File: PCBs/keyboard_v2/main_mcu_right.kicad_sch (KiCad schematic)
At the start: 28 parts, among them U801 STM32U5G9ZJJ6Q, U802 M24256X-FCU6T_VF, Y801 16MHz

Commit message: V2 progress
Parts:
- removed C801, C802: 6p, Capacitor_SMD:C_0402_1005Metric, symbol Device:C_Small
- removed Y801: 16MHz, Crystal:Crystal_SMD_2016-4Pin_2.0x1.6mm, symbol Device:Crystal_GND24_Small
- added C823, C824: 12p, Capacitor_SMD:C_0402_1005Metric, symbol Device:C_Small
- added Y802: 32MHz, Crystal:Crystal_SMD_2016-4Pin_2.0x1.6mm, symbol Device:Crystal_GND24_Small
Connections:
- net GND: now also C823.1, C824.1, Y802.2, Y802.4
- net OSC_IN: now also C823.2, Y802.3
- net OSC_OUT: now also C824.2, Y802.1
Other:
- moved on the sheet: U801B

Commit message: V2 Progress
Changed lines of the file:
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@@
+		)
+	)
+	(hierarchical_label "DSI_D0P"
+		(shape bidirectional)
+		(at 185.42 139.7 0)
+		(fields_autoplaced yes)
+		(effects
+			(font
+				(size 1.27 1.27)
+			)
+			(justify left)
 		)
 	)
@@
 		)
 	)
+	(hierarchical_label "DSI_CKN"
+		(shape output)
+		(at 185.42 137.16 0)
+		(fields_autoplaced yes)
+		(effects
+			(font
+				(size 1.27 1.27)
+			)
+			(justify left)
+		)
+	)
 	(hierarchical_label "KEY_B11"
 		(shape input)
@@
 		)
 	)
+	(hierarchical_label "DSI_TE"
+		(shape input)
+		(at 185.42 132.08 0)
+		(fields_autoplaced yes)
+		(effects
+			(font
+				(size 1.27 1.27)
+			)
+			(justify left)
+		)
+	)
 	(hierarchical_label "KEY_A11"
 		(shape input)
@@
 		)
 	)
+	(hierarchical_label "USB_DN"
+		(shape bidirectional)
+		(at 185.42 119.38 0)
+		(fields_autoplaced yes)
+		(effects
+			(font
+				(size 1.27 1.27)
+			)
+			(justify left)
+		)
+	)
 	(hierarchical_label "KEY_A10"
 		(shape input)
@@
 		)
 	)
+	(hierarchical_label "DSI_D0N"
+		(shape bidirectional)
+		(at 185.42 142.24 0)
+		(fields_autoplaced yes)
+		(effects
+			(font
+				(size 1.27 1.27)
+			)
+			(justify left)
+		)
+	)
 	(hierarchical_label "KEY_A12"
 		(shape input)
@@
 		)
 	)
+	(hierarchical_label "USB_DP"
+		(shape bidirectional)
+		(at 185.42 116.84 0)
+		(fields_autoplaced yes)
+		(effects
+			(font
+				(size 1.27 1.27)
+			)
+			(justify left)
+		)
+	)
 	(hierarchical_label "KEY_B10"
 		(shape input)
@@
 		(fields_autoplaced yes)
 		(effects
+			(font
+				(size 1.27 1.27)
+			)
+			(justify left)
+		)
+	)
+	(hierarchical_label "DSI_CKP"
+		(shape output)
+		(at 185.42 134.62 0)
+		(fields_autoplaced yes)
+		(effects

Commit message: Display schematic done
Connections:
- net +1V8: now also U802.A1 (VCC); no longer U801.E6 (VDDIO2)
- net +3V3: now also U801.E6 (VDDIO2); no longer U802.A1 (VCC)
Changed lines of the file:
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@@
 	)
 	(junction
+		(at 205.74 226.06)
+		(diameter 0)
+		(color 0 0 0 0)
+	)
+	(junction
 		(at 195.58 233.68)
 		(diameter 0)
@@
 	)
 	(junction
+		(at 205.74 218.44)
+		(diameter 0)
+		(color 0 0 0 0)
+	)
+	(junction
 		(at 256.54 215.9)
 		(diameter 0)
@@
 	)
 	(junction
-		(at 205.74 226.06)
-		(diameter 0)
-		(color 0 0 0 0)
-	)
-	(junction
 		(at 53.34 246.38)
 		(diameter 0)
@@
 	)
 	(junction
-		(at 205.74 218.44)
-		(diameter 0)
-		(color 0 0 0 0)
-	)
-	(junction
 		(at 256.54 243.84)
 		(diameter 0)
@@
 	)
 	(junction
-		(at 205.74 223.52)
-		(diameter 0)
-		(color 0 0 0 0)
-	)
-	(junction
 		(at 205.74 233.68)
 		(diameter 0)
@@
 	(wire
 		(pts
+			(xy 205.74 226.06) (xy 205.74 228.6)
+		)
+		(stroke
+			(width 0)
+			(type default)
+		)
+	)
+	(wire
+		(pts
 			(xy 256.54 205.74) (xy 254 205.74)
 		)
@@
 	(wire
 		(pts
+			(xy 208.28 226.06) (xy 205.74 226.06)
+		)
+		(stroke
+			(width 0)
+			(type default)
+		)
+	)
+	(wire
+		(pts
 			(xy 256.54 218.44) (xy 256.54 220.98)
 		)
@@
 	(wire
 		(pts
-			(xy 205.74 226.06) (xy 205.74 228.6)
-		)
-		(stroke
-			(width 0)
-			(type default)
-		)
-	)
-	(wire
-		(pts
 			(xy 256.54 200.66) (xy 254 200.66)
 		)
@@
 	(wire
 		(pts
-			(xy 205.74 223.52) (xy 205.74 226.06)
-		)
-		(stroke
-			(width 0)
-			(type default)
-		)
-	)
-	(wire
-		(pts
 			(xy 386.08 238.76) (xy 388.62 238.76)
 		)
@@
 	(wire
 		(pts
+			(xy 200.66 223.52) (xy 208.28 223.52)
+		)
+		(stroke
+			(width 0)
+			(type default)
+		)
+	)
+	(wire
+		(pts
 			(xy 205.74 205.74) (xy 208.28 205.74)
 		)
@@
 	(wire
 		(pts
-			(xy 205.74 223.52) (xy 208.28 223.52)
+			(xy 205.74 218.44) (xy 205.74 226.06)
 		)
 		(stroke
@@
 	(wire
 		(pts
+			(xy 200.66 220.98) (xy 200.66 223.52)
+		)
+		(stroke
+			(width 0)
+			(type default)
+		)
+	)
+	(wire
+		(pts
 			(xy 256.54 228.6) (xy 256.54 233.68)
 		)
@@
 	(wire
 		(pts
-			(xy 205.74 218.44) (xy 205.74 223.52)
-		)
-		(stroke
-			(width 0)
-			(type default)
-		)
-	)
-	(wire
-		(pts
 			(xy 73.66 220.98) (xy 83.82 220.98)
 		)
@@
 	(wire
 		(pts
-			(xy 205.74 226.06) (xy 208.28 226.06)
-		)
-		(stroke
-			(width 0)
-			(type default)
-		)
-	)
-	(wire
-		(pts
 			(xy 63.5 254) (xy 63.5 256.54)
 		)
@@
 	(symbol
 		(lib_id "power:+3V3")
+		(at 200.66 220.98 0)
+		(unit 1)
+		(exclude_from_sim no)
+		(in_bom yes)
+		(on_board yes)
+		(dnp no)
+		(fields_autoplaced yes)
+		(property "Reference" "#PWR0805"
+			(at 200.66 224.79 0)
+			(effects
+				(font
+					(size 1.27 1.27)
+				)
+				(hide yes)
+			)
+		)
+		(property "Value" "+3V3"
+			(at 200.66 217.17 0)
+			(effects
+				(font
+					(size 1.27 1.27)
+				)
+			)
+		)
+		(property "Footprint" ""
+			(at 200.66 220.98 0)
+			(effects
+				(font
+					(size 1.27 1.27)
+				)
+				(hide yes)
+			)
+		)
+		(property "Datasheet" ""
+			(at 200.66 220.98 0)
+			(effects
+				(font
+					(size 1.27 1.27)
+				)
+				(hide yes)
+			)
+		)
+		(property "Description" "Power symbol creates a global label with name \"+3V3\""
+			(at 200.66 220.98 0)
+			(effects
+				(font
+					(size 1.27 1.27)
+				)
+				(hide yes)
+			)
+		)
+		(pin "1"
+		)
+		(instances
+			(project "keyboard_v2"
+				(path "/e2360b7f-be71-48d9-b398-9f8cd45479d6/b599252a-0e44-4760-9c79-385d4380db60/c45c2f49-4b68-419d-a43d-2f217736a467"
+					(reference "#PWR0805")
+					(unit 1)
+				)
+			)
+		)
+	)
+	(symbol
+		(lib_id "power:+3V3")
 		(at 251.46 40.64 0)
 		(unit 1)
@@
 	)
 	(symbol
+		(lib_id "power:+1V8")
+		(at 388.62 233.68 0)
+		(mirror y)
+		(unit 1)
+		(exclude_from_sim no)
+		(in_bom yes)
+		(on_board yes)
+		(dnp no)
+		(fields_autoplaced yes)
+		(property "Reference" "#PWR0803"
+			(at 388.62 237.49 0)
+			(effects
+				(font
+					(size 1.27 1.27)
+				)
+				(hide yes)
+			)
+		)
+		(property "Value" "+1V8"
+			(at 388.62 228.6 0)
+			(effects
+				(font
+					(size 1.27 1.27)
+				)
+			)
+		)
+		(property "Footprint" ""
+			(at 388.62 233.68 0)
+			(effects
+				(font
+					(size 1.27 1.27)
+				)
+				(hide yes)
+			)
+		)
+		(property "Datasheet" ""
+			(at 388.62 233.68 0)
+			(effects
+				(font
+					(size 1.27 1.27)
+				)
+				(hide yes)
+			)
+		)
+		(property "Description" "Power symbol creates a global label with name \"+1V8\""
+			(at 388.62 233.68 0)
+			(effects
+				(font
+					(size 1.27 1.27)
+				)
+				(hide yes)
+			)
+		)
+		(pin "1"
+		)
+		(instances
+			(project "keyboard_v2"
+				(path "/e2360b7f-be71-48d9-b398-9f8cd45479d6/b599252a-0e44-4760-9c79-385d4380db60/c45c2f49-4b68-419d-a43d-2f217736a467"
+					(reference "#PWR0803")
+					(unit 1)
+				)
+			)
+		)
+	)
+	(symbol
 		(lib_id "M24256X-FCU6T_VF:M24256X-FCU6T_VF")
 		(at 373.38 236.22 0)
@@
 					(unit 1)
 				)
-			)
-		)
-	)
-	(symbol
-		(lib_id "power:+3V3")
-		(at 388.62 233.68 0)
-		(unit 1)
-		(exclude_from_sim no)
-		(in_bom yes)
-		(on_board yes)
-		(dnp no)
-		(fields_autoplaced yes)
-		(property "Reference" "#PWR0803"
-			(at 388.62 237.49 0)
-			(effects
-				(font
-					(size 1.27 1.27)
-				)
-				(hide yes)
-			)
-		)
-		(property "Value" "+3V3"
-			(at 388.62 228.6 0)
-			(effects
-				(font
-					(size 1.27 1.27)
-				)
-			)
-		)
-		(property "Footprint" ""
-			(at 388.62 233.68 0)
-			(effects
-				(font
-					(size 1.27 1.27)
-				)
-				(hide yes)
-			)
-		)
-		(property "Datasheet" ""
-			(at 388.62 233.68 0)
-			(effects
-				(font
-					(size 1.27 1.27)
-				)
-				(hide yes)
-			)
-		)
-		(property "Description" "Power symbol creates a global label with name \"+3V3\""
-			(at 388.62 233.68 0)
-			(effects
-				(font
-					(size 1.27 1.27)
-				)
-				(hide yes)
-			)
-		)
-		(pin "1"
-		)
-		(instances
-			(project "keyboard_v2"
-				(path "/e2360b7f-be71-48d9-b398-9f8cd45479d6/b599252a-0e44-4760-9c79-385d4380db60/c45c2f49-4b68-419d-a43d-2f217736a467"
-					(reference "#PWR0803")
-					(unit 1)
-				)

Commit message: V2 Schematic mostly done
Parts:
- U802: footprint watch_footprints:BGA4C50P2X2_70X98X33 -> keyboard_footprints:BGA4C50P2X2_70X98X33
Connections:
- net +1V8: now also R801.1, R802.1; no longer C813.1, C815.1
- net +3V3: now also C813.1, C815.1; no longer R801.1, R802.1
- net DSI_CKN: now also U801.F1 (DSI_CKN)
- net DSI_CKP: now also U801.F2 (DSI_CKP)
- net DSI_D0N: now also U801.E1 (DSI_D0N)
- net DSI_D0P: now also U801.E2 (DSI_D0P)
- net OSC_IN: now also U801.H2 (PH0-OSC_IN)
- net OSC_OUT: now also U801.J1 (PH1-OSC_OUT)
- net RST: now also U801.J2 (NRST)
- no-connect marks 0 -> 2
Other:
- note added: "ENCODER PINS MUST BE 5V TOLERANT"
- moved on the sheet: U801B

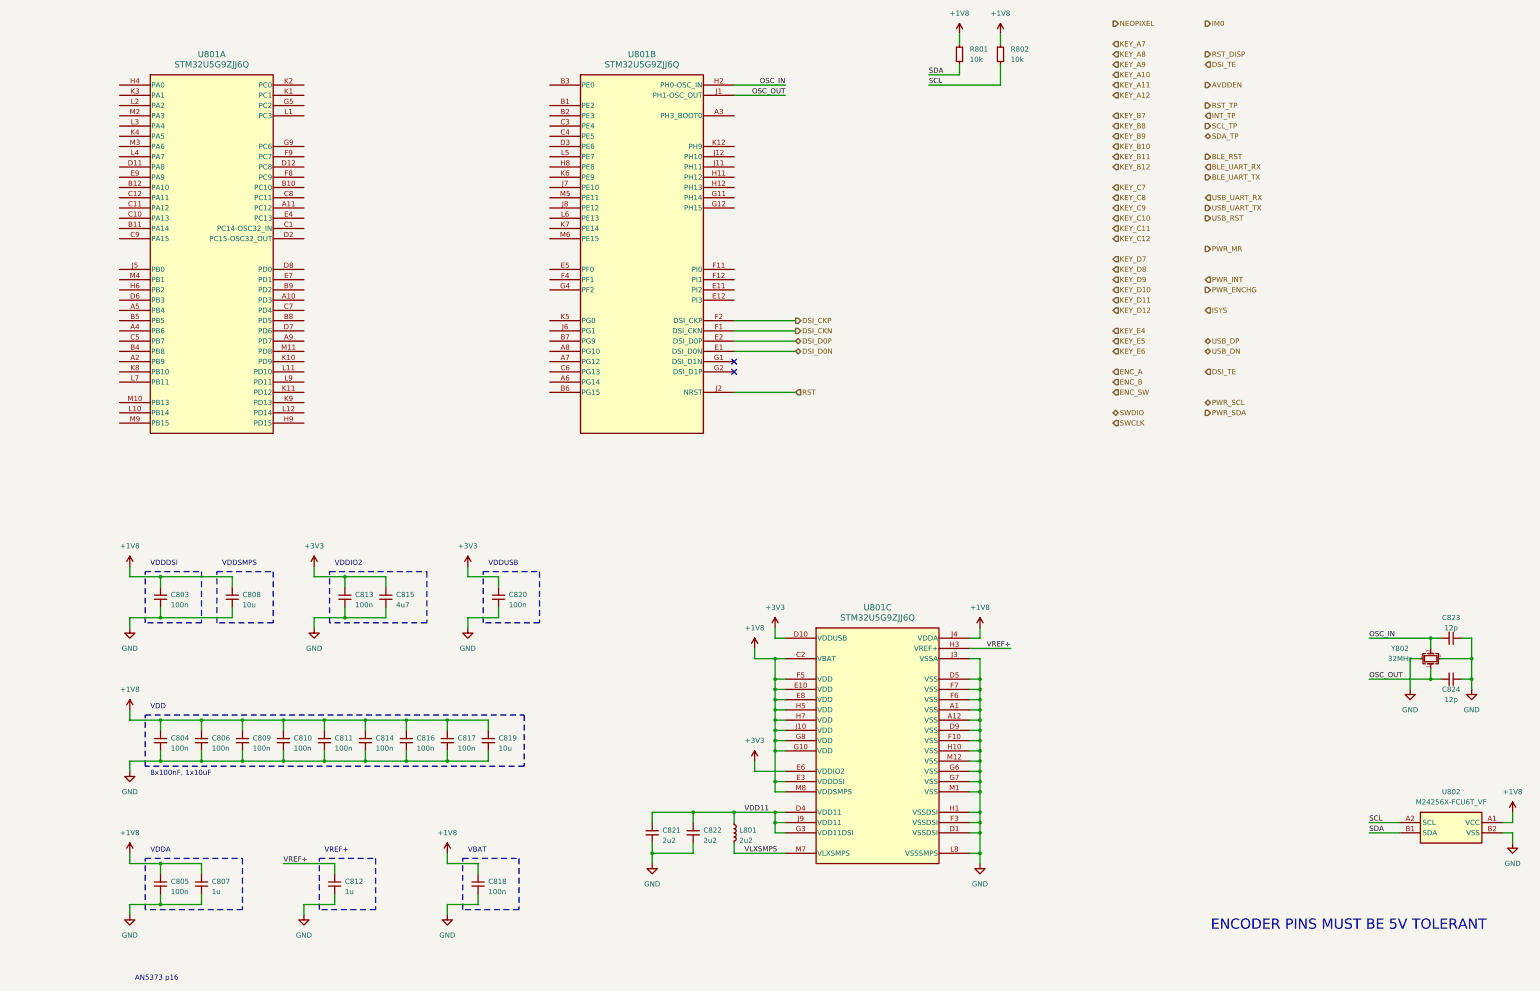
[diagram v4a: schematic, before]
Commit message: Schematic mostly done, moving onto PCB
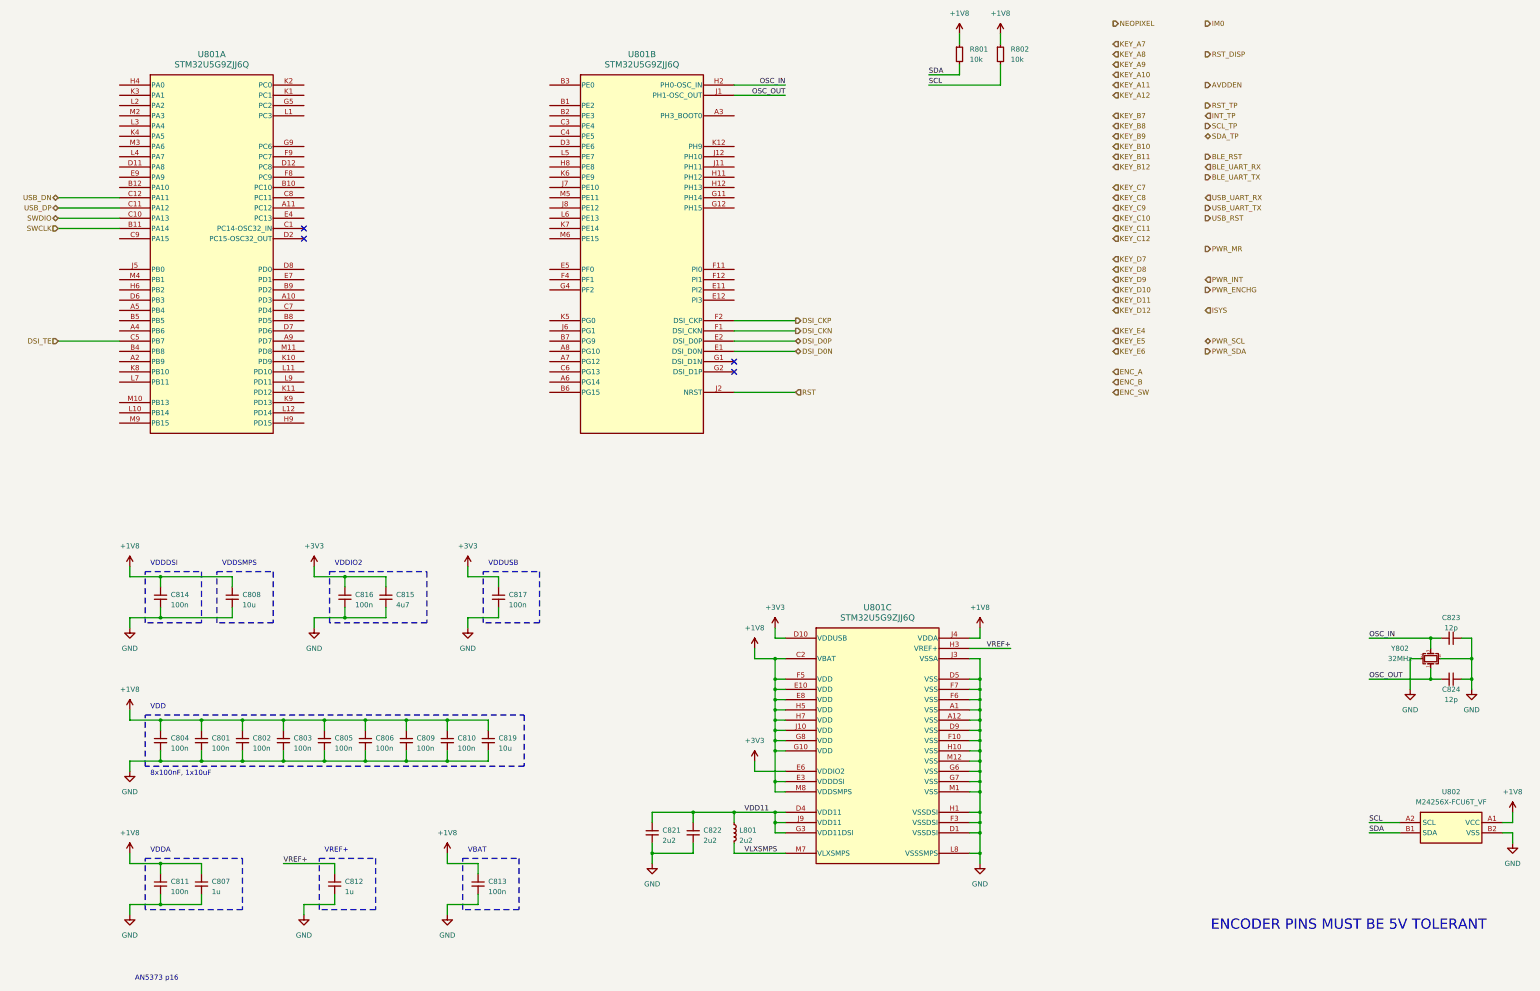
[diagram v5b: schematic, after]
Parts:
- removed C818, C820: 100n, Capacitor_SMD:C_0201_0603Metric, symbol Device:C_Small
- added C801, C802: 100n, Capacitor_SMD:C_0402_1005Metric, symbol Device:C_Small
- C803, C804, C805, C806, C809, C810, C811, C812, C813, C814, C816, C817, C821, C822: footprint Capacitor_SMD:C_0201_0603Metric -> Capacitor_SMD:C_0402_1005Metric
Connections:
- net +1V8: now also C813.1, C801.1, C802.1; no longer C816.1, C817.1
- net +3V3: now also C816.1, C817.1; no longer C813.1
- net DSI_TE: now also U801.C5 (PB7)
- net GND: now also C801.2, C802.2
- net SWCLK: now also U801.B11 (PA14)
- net SWDIO: now also U801.C10 (PA13)
- net USB_DN: now also U801.C12 (PA11)
- net USB_DP: now also U801.C11 (PA12)
- no-connect marks 2 -> 4

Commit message: Placement done
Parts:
- C807: footprint Capacitor_SMD:C_0201_0603Metric -> Capacitor_SMD:C_0402_1005Metric
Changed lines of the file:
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@@
 			)
 		)
-		(property "Footprint" "Capacitor_SMD:C_0201_0603Metric"
+		(property "Footprint" "Capacitor_SMD:C_0402_1005Metric"
 			(at 63.5 251.46 0)
 			(effects

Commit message: 279 Unrouted
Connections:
- net SCL is gone; now on net PWR_SCL: R802.2, U802.A2 (SCL)
- net SDA is gone; now on net PWR_SDA: R801.2, U802.B1 (SDA)
- net AVDDEN: now also U801.L1 (PC3)
- net BLE_UART_RX: now also U801.K10 (PD9)
- net BLE_UART_TX: now also U801.M11 (PD8)
- net IM0: now also U801.B1 (PE2)
- net INT_TP: now also U801.L2 (PA2)
- net NEOPIXEL: now also U801.M9 (PB15)
- net RST_DISP: now also U801.K2 (PC0)
- net RST_TP: now also U801.A7 (PG12)
- net SCL_TP: now also U801.A6 (PG14)
- net SDA_TP: now also U801.C6 (PG13)
- no-connect marks 4 -> 5
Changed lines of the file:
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@@
+	)
+	(no_connect
+		(at 43.18 132.08)
 	)
 	(no_connect
@@
 	(wire
 		(pts
+			(xy 88.9 60.96) (xy 99.06 60.96)
+		)
+		(stroke
+			(width 0)
+			(type default)
+		)
+	)
+	(wire
+		(pts
 			(xy 63.5 210.82) (xy 73.66 210.82)
 		)
@@
 	(wire
 		(pts
+			(xy 88.9 121.92) (xy 101.6 121.92)
+		)
+		(stroke
+			(width 0)
+			(type default)
+		)
+	)
+	(wire
+		(pts
+			(xy 325.12 119.38) (xy 335.28 119.38)
+		)
+		(stroke
+			(width 0)
+			(type default)
+		)
+	)
+	(wire
+		(pts
 			(xy 185.42 233.68) (xy 185.42 236.22)
 		)
@@
 	(wire
 		(pts
+			(xy 139.7 124.46) (xy 149.86 124.46)
+		)
+		(stroke
+			(width 0)
+			(type default)
+		)
+	)
+	(wire
+		(pts
 			(xy 45.72 220.98) (xy 53.34 220.98)
 		)
@@
 	(wire
 		(pts
+			(xy 27.94 137.16) (xy 43.18 137.16)
+		)
+		(stroke
+			(width 0)
+			(type default)
+		)
+	)
+	(wire
+		(pts
 			(xy 205.74 195.58) (xy 205.74 200.66)
 		)
@@
 	(wire
 		(pts
+			(xy 139.7 127) (xy 149.86 127)
+		)
+		(stroke
+			(width 0)
+			(type default)
+		)
+	)
+	(wire
+		(pts
 			(xy 386.08 238.76) (xy 388.62 238.76)
 		)
@@
 	(wire
 		(pts
+			(xy 137.16 58.42) (xy 149.86 58.42)
+		)
+		(stroke
+			(width 0)
+			(type default)
+		)
+	)
+	(wire
+		(pts
 			(xy 88.9 256.54) (xy 96.52 256.54)
 		)
@@
 	(wire
 		(pts
+			(xy 27.94 58.42) (xy 43.18 58.42)
+		)
+		(stroke
+			(width 0)
+			(type default)
+		)
+	)
+	(wire
+		(pts
 			(xy 114.3 210.82) (xy 124.46 210.82)
 		)
@@
 	(wire
 		(pts
+			(xy 325.12 116.84) (xy 335.28 116.84)
+		)
+		(stroke
+			(width 0)
+			(type default)
+		)
+	)
+	(wire
+		(pts
 			(xy 200.66 223.52) (xy 208.28 223.52)
 		)
@@
 	(wire
 		(pts
+			(xy 88.9 119.38) (xy 101.6 119.38)
+		)
+		(stroke
+			(width 0)
+			(type default)
+		)
+	)
+	(wire
+		(pts
 			(xy 363.22 195.58) (xy 365.76 195.58)
 		)
@@
 	(wire
 		(pts
+			(xy 88.9 53.34) (xy 99.06 53.34)
+		)
+		(stroke
+			(width 0)
+			(type default)
+		)
+	)
+	(wire
+		(pts
 			(xy 114.3 210.82) (xy 114.3 213.36)
 		)
@@
 		(pts
 			(xy 93.98 220.98) (xy 104.14 220.98)
+		)
+		(stroke
+			(width 0)
+			(type default)
+		)
+	)
+	(wire
+		(pts
+			(xy 139.7 121.92) (xy 149.86 121.92)
 		)
 		(stroke
@@
 		)
 	)
+	(label "SCL"
+		(at 327.66 116.84 0)
+		(fields_autoplaced yes)
+		(effects
+			(font
+				(size 1.27 1.27)
+			)
+			(justify left bottom)
+		)
+	)
+	(label "SDA"
+		(at 327.66 119.38 0)
+		(fields_autoplaced yes)
+		(effects
+			(font
+				(size 1.27 1.27)
+			)
+			(justify left bottom)
+		)
+	)
 	(label "OSC_IN"
 		(at 208.28 53.34 180)
@@
 	(hierarchical_label "NEOPIXEL"
 		(shape output)
-		(at 289.56 38.1 0)
-		(fields_autoplaced yes)
-		(effects
-			(font
-				(size 1.27 1.27)
-			)
-			(justify left)
+		(at 27.94 137.16 180)
+		(fields_autoplaced yes)
+		(effects
+			(font
+				(size 1.27 1.27)
+			)
+			(justify right)
 		)
 	)
 	(hierarchical_label "SDA_TP"
 		(shape bidirectional)
-		(at 312.42 66.04 0)
-		(fields_autoplaced yes)
-		(effects
-			(font
-				(size 1.27 1.27)
-			)
-			(justify left)
+		(at 139.7 124.46 180)
+		(fields_autoplaced yes)
+		(effects
+			(font
+				(size 1.27 1.27)
+			)
+			(justify right)
 		)
 	)
@@
 	(hierarchical_label "BLE_UART_RX"
 		(shape input)
-		(at 312.42 73.66 0)
+		(at 101.6 121.92 0)
 		(fields_autoplaced yes)
 		(effects
@@
 	(hierarchical_label "RST_TP"
 		(shape output)
-		(at 312.42 58.42 0)
-		(fields_autoplaced yes)
-		(effects
-			(font
-				(size 1.27 1.27)
-			)
-			(justify left)
+		(at 139.7 121.92 180)
+		(fields_autoplaced yes)
+		(effects
+			(font
+				(size 1.27 1.27)
+			)
+			(justify right)
 		)
 	)
@@
 	(hierarchical_label "PWR_SDA"
 		(shape output)
-		(at 312.42 119.38 0)
-		(fields_autoplaced yes)
-		(effects
-			(font
-				(size 1.27 1.27)
-			)
-			(justify left)
+		(at 325.12 119.38 180)
+		(fields_autoplaced yes)
+		(effects
+			(font
+				(size 1.27 1.27)
+			)
+			(justify right)
 		)
 	)
@@
 	(hierarchical_label "AVDDEN"
 		(shape output)
-		(at 312.42 53.34 0)
+		(at 99.06 60.96 0)
 		(fields_autoplaced yes)
 		(effects
@@
 	(hierarchical_label "BLE_UART_TX"
 		(shape output)
-		(at 312.42 76.2 0)
+		(at 101.6 119.38 0)
 		(fields_autoplaced yes)
 		(effects
@@
 	(hierarchical_label "PWR_SCL"
 		(shape bidirectional)
-		(at 312.42 116.84 0)
-		(fields_autoplaced yes)
-		(effects
-			(font
-				(size 1.27 1.27)
-			)
-			(justify left)
+		(at 325.12 116.84 180)
+		(fields_autoplaced yes)
+		(effects
+			(font
+				(size 1.27 1.27)
+			)
+			(justify right)
 		)
 	)
@@
 	(hierarchical_label "INT_TP"
 		(shape input)
-		(at 312.42 60.96 0)
-		(fields_autoplaced yes)
-		(effects
-			(font
-				(size 1.27 1.27)
-			)
-			(justify left)
+		(at 27.94 58.42 180)
+		(fields_autoplaced yes)
+		(effects
+			(font
+				(size 1.27 1.27)
+			)
+			(justify right)
 		)
 	)
@@
 	(hierarchical_label "RST_DISP"
 		(shape output)
-		(at 312.42 45.72 0)
+		(at 99.06 53.34 0)
 		(fields_autoplaced yes)
 		(effects
@@
 	(hierarchical_label "SCL_TP"
 		(shape output)
-		(at 312.42 63.5 0)
-		(fields_autoplaced yes)
-		(effects
-			(font
-				(size 1.27 1.27)
-			)
-			(justify left)
+		(at 139.7 127 180)
+		(fields_autoplaced yes)
+		(effects
+			(font
+				(size 1.27 1.27)
+			)
+			(justify right)
 		)
 	)
@@
 	(hierarchical_label "IM0"
 		(shape output)
-		(at 312.42 38.1 0)
-		(fields_autoplaced yes)
-		(effects
-			(font
-				(size 1.27 1.27)
-			)
-			(justify left)
-		)
-	)
+		(at 137.16 58.42 180)
+		(fields_autoplaced yes)
+		(effects
+			(font
+				(size 1.27 1.27)
+			)
+			(justify right)
+		)
+	)
